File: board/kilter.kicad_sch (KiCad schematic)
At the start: 51 parts, among them J1 IN1, J2 HP, J3 IN2, J4 LP, J5 BP, J6 POWER, J7 NOTCH, U1 TL074, U2 TL072, U3 TL074, U4 LM4040C5

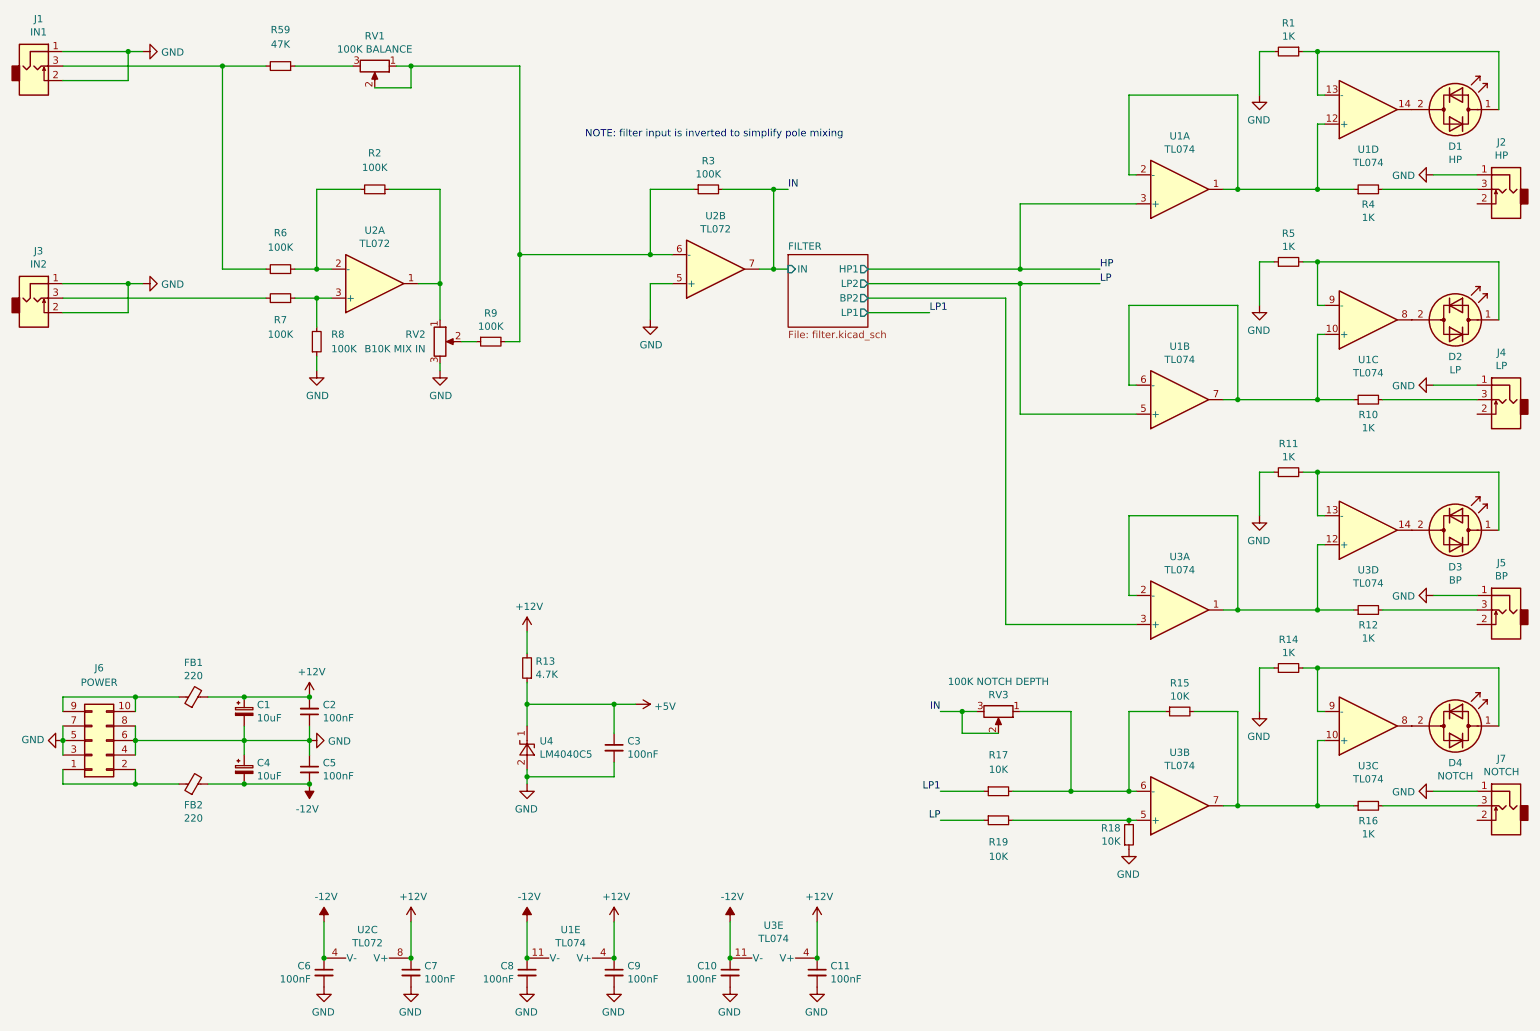
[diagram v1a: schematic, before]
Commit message: fix resonance gain and simplify module calibration
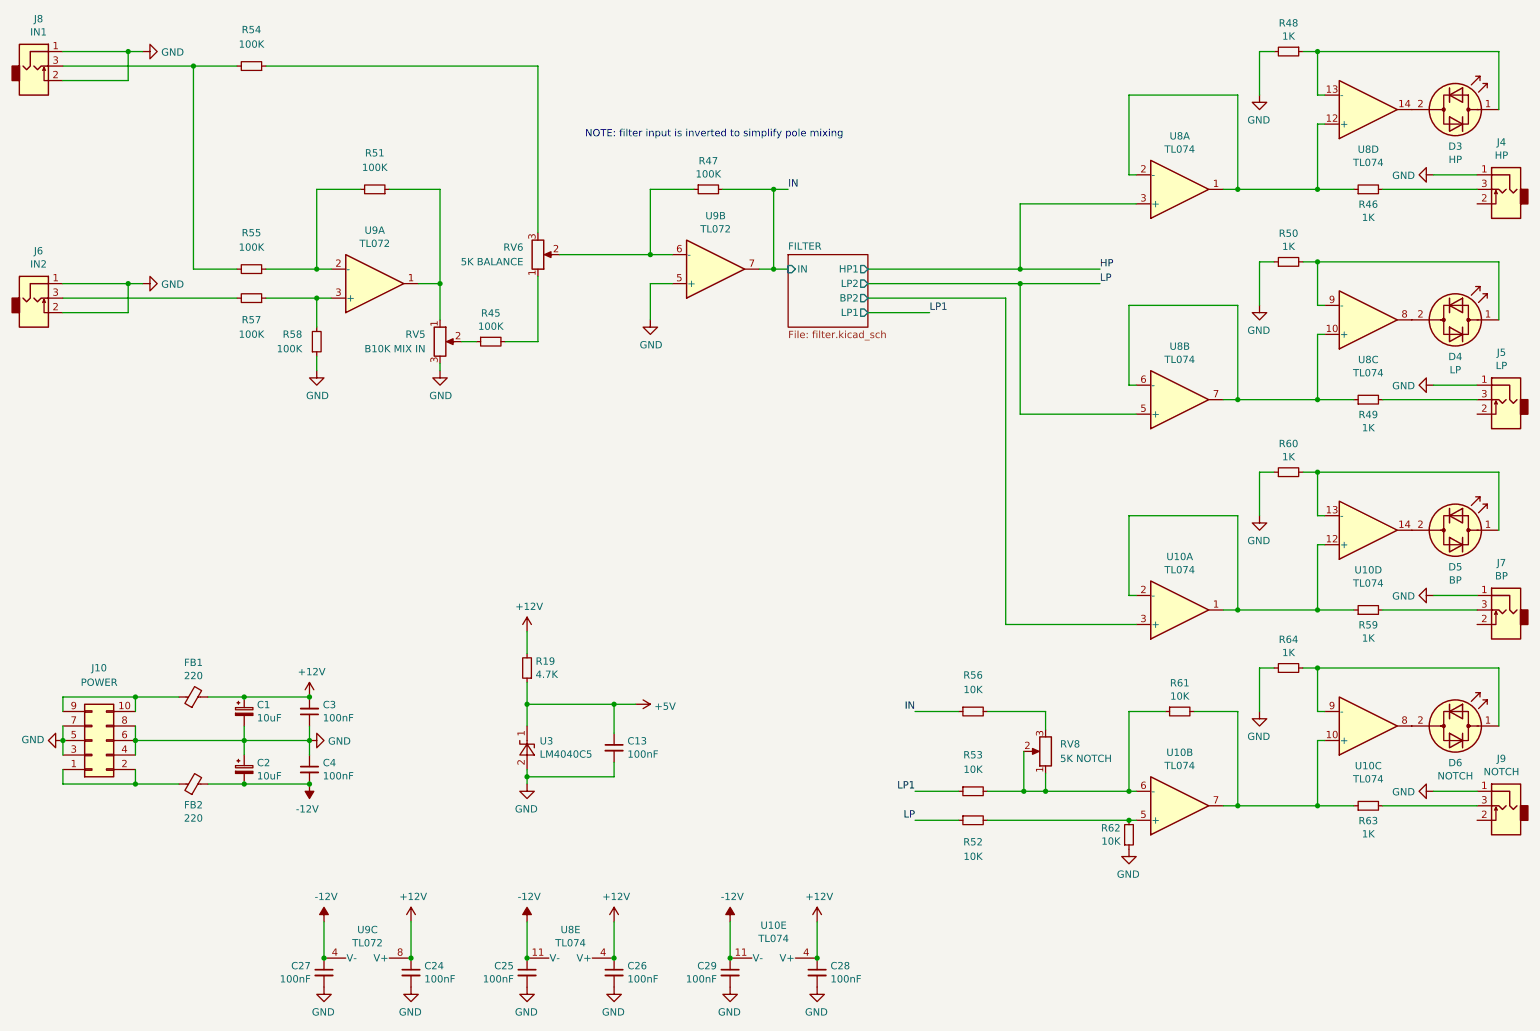
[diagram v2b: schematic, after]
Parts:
- removed RV1: 100K BALANCE, Potentiometer_SMD:Potentiometer_Bourns_TC33X_Vertical, symbol vcf-20-rescue:R_POT-Device
- added R56: 10K, Resistor_SMD:R_0603_1608Metric, symbol Device:R_Small
- added RV6: 5K BALANCE, Potentiometer_SMD:Potentiometer_Bourns_TC33X_Vertical, symbol vcf-20-rescue:R_POT-Device
- R54: renamed from R59; value 47K -> 100K
- RV8: renamed from RV3; value 100K NOTCH DEPTH -> 5K NOTCH
- renumbered C3 to C13, C4 to C2, C7 to C24, C8 to C25, C9 to C26, C6 to C27, C11 to C28, C10 to C29, C2 to C3, C5 to C4, D1 to D3, D2 to D4, D3 to D5, D4 to D6, J6 to J10, J2 to J4, J4 to J5, J3 to J6, J5 to J7, J1 to J8, J7 to J9, R13 to R19, R9 to R45, R4 to R46, R3 to R47, R1 to R48, R10 to R49, R5 to R50, R2 to R51, R19 to R52, R17 to R53, R6 to R55, R7 to R57, R8 to R58, R12 to R59, R11 to R60, R15 to R61, R18 to R62, R16 to R63, R14 to R64, RV2 to RV5, U3 to U10, U4 to U3, U1 to U8, U2 to U9
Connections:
- net IN: now also R56.1; no longer RV8.2, RV8.3
- net at R47.1, U9.6 (-): now also RV6.2; no longer R45.2
- net at R53.2, R61.1, RV8.1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: now also RV8.2
- net at R54.1: now also RV6.3
- new net: R56.2, RV8.3
- new net: R45.2, RV6.1
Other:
- moved on the sheet: R52, R53, R54, R55, R57, RV8

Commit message: fix back silkscreen and update production files
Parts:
- C1, C2: LCSC (none) -> C178621
- C13, C24, C25, C26, C27, C28, C29, C3, C4: LCSC (none) -> C14663
- FB1, FB2: LCSC (none) -> C88988
- R19: LCSC (none) -> C23162
- R45, R47, R51, R54, R55, R57, R58: LCSC (none) -> C25803
- R46, R48, R49, R50, R59, R60, R63, R64: LCSC (none) -> C21190
- R52, R53, R56, R61, R62: LCSC (none) -> C25804
- RV6, RV8: LCSC (none) -> C719177
- U10, U8: LCSC (none) -> C96507
- U3: LCSC (none) -> C156291
- U9: LCSC (none) -> C90748
